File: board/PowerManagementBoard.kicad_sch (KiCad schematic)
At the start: 0 parts

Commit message: Added Hierarchys
Voltage sensing sheet
Reverse Current Protection Sheet
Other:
- added sheet Current Protection (CurrentProtection.kicad_sch)
- added sheet Voltage Sensing (Voltage_Sensing.kicad_sch)
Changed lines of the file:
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@@
 	(generator_version "9.0")
 	(paper "A4")
+	(sheet
+		(at 22.86 72.39)
+		(size 44.45 33.02)
+		(exclude_from_sim no)
+		(in_bom yes)
+		(on_board yes)
+		(dnp no)
+		(fields_autoplaced yes)
+		(stroke
+			(width 0.1524)
+			(type solid)
+		)
+		(fill
+			(color 0 0 0 0.0000)
+		)
+		(property "Sheetname" "Voltage Sensing"
+			(at 22.86 71.6784 0)
+			(effects
+				(font
+					(size 1.27 1.27)
+				)
+				(justify left bottom)
+			)
+		)
+		(property "Sheetfile" "Voltage_Sensing.kicad_sch"
+			(at 22.86 105.9946 0)
+			(effects
+				(font
+					(size 1.27 1.27)
+				)
+				(justify left top)
+			)
+		)
+		(instances
+			(project "PowerManagementBoard"
+				(path "/7eaa639d-7062-45e7-be05-1c2855431307"
+					(page "3")
+				)
+			)
+		)
+	)
+	(sheet
+		(at 21.59 25.4)
+		(size 45.72 33.02)
+		(exclude_from_sim no)
+		(in_bom yes)
+		(on_board yes)
+		(dnp no)
+		(fields_autoplaced yes)
+		(stroke
+			(width 0.1524)
+			(type solid)
+		)
+		(fill
+			(color 0 0 0 0.0000)
+		)
+		(property "Sheetname" "Current Protection"
+			(at 21.59 24.6884 0)
+			(effects
+				(font
+					(size 1.27 1.27)
+				)
+				(justify left bottom)
+			)
+		)
+		(property "Sheetfile" "CurrentProtection.kicad_sch"
+			(at 21.59 59.0046 0)
+			(effects
+				(font
+					(size 1.27 1.27)
+				)
+				(justify left top)
+			)
+		)
+		(instances
+			(project "PowerManagementBoard"
+				(path "/7eaa639d-7062-45e7-be05-1c2855431307"
+					(page "2")
+				)
+			)
+		)
+	)
 	(sheet_instances
 		(path "/"

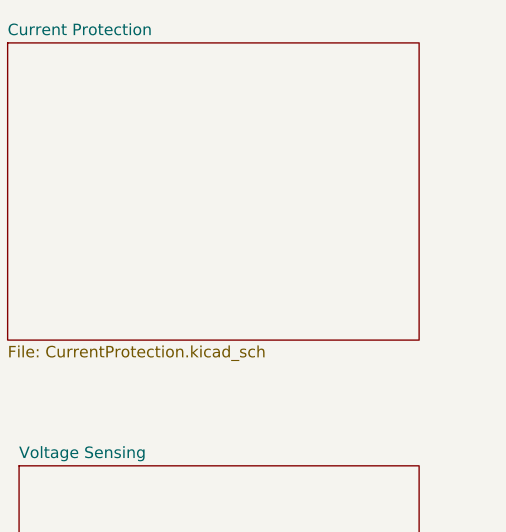
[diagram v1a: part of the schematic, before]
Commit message: Resistor Values
Added resistor values for everything on voltage sensing circuit
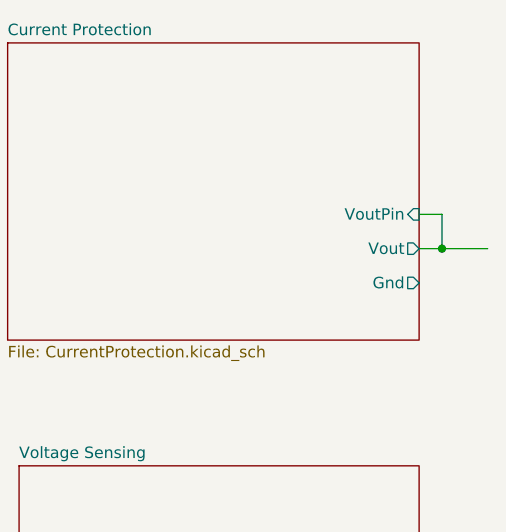
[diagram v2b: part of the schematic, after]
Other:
- sheet Current Protection ports: added Gnd, Vout, VoutPin; removed none
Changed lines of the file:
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@@
 	(generator_version "9.0")
 	(paper "A4")
+	(junction
+		(at 69.85 48.26)
+		(diameter 0)
+		(color 0 0 0 0)
+	)
+	(wire
+		(pts
+			(xy 69.85 48.26) (xy 69.85 44.45)
+		)
+		(stroke
+			(width 0)
+			(type default)
+		)
+	)
+	(wire
+		(pts
+			(xy 67.31 48.26) (xy 69.85 48.26)
+		)
+		(stroke
+			(width 0)
+			(type default)
+		)
+	)
+	(wire
+		(pts
+			(xy 69.85 48.26) (xy 74.93 48.26)
+		)
+		(stroke
+			(width 0)
+			(type default)
+		)
+	)
+	(wire
+		(pts
+			(xy 69.85 44.45) (xy 67.31 44.45)
+		)
+		(stroke
+			(width 0)
+			(type default)
+		)
+	)
 	(sheet
 		(at 22.86 72.39)
@@
 			)
 		)
+		(pin "Gnd" output
+			(at 67.31 52.07 0)
+			(effects
+				(font
+					(size 1.27 1.27)
+				)
+				(justify right)
+			)
+		)
+		(pin "Vout" output
+			(at 67.31 48.26 0)
+			(effects
+				(font
+					(size 1.27 1.27)
+				)
+				(justify right)
+			)
+		)
+		(pin "VoutPin" input
+			(at 67.31 44.45 0)
+			(effects
+				(font
+					(size 1.27 1.27)
+				)
+				(justify right)
+			)
+		)

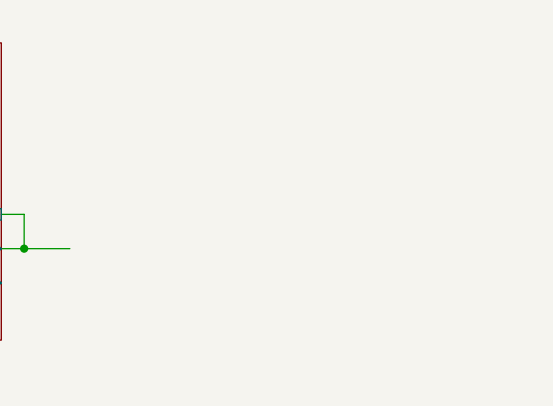
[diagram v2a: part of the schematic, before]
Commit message: fix switch page not showing up
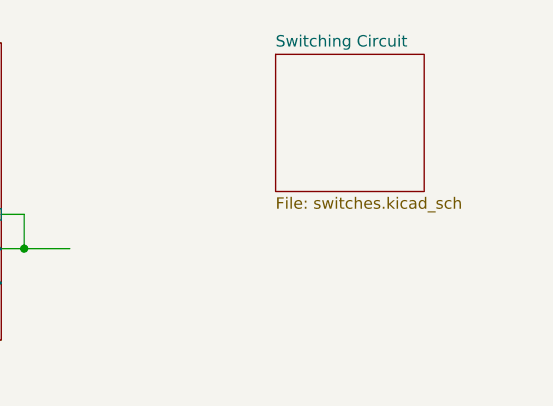
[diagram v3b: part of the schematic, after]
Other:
- added sheet Switching Circuit (switches.kicad_sch)
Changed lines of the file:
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@@
+	)
+	(sheet
+		(at 97.79 26.67)
+		(size 16.51 15.24)
+		(exclude_from_sim no)
+		(in_bom yes)
+		(on_board yes)
+		(dnp no)
+		(fields_autoplaced yes)
+		(stroke
+			(width 0.1524)
+			(type solid)
+		)
+		(fill
+			(color 0 0 0 0.0000)
+		)
+		(property "Sheetname" "Switching Circuit"
+			(at 97.79 25.9584 0)
+			(effects
+				(font
+					(size 1.27 1.27)
+				)
+				(justify left bottom)
+			)
+		)
+		(property "Sheetfile" "switches.kicad_sch"
+			(at 97.79 42.4946 0)
+			(effects
+				(font
+					(size 1.27 1.27)
+				)
+				(justify left top)
+			)
+		)
+		(instances
+			(project "PowerManagementBoard"
+				(path "/7eaa639d-7062-45e7-be05-1c2855431307"
+					(page "4")
+				)
+			)
+		)
 	)
 	(sheet

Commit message: Changed Flags
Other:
- sheet Current Protection ports: added none; removed Gnd, VoutPin
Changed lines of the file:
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@@
 	(generator_version "9.0")
 	(paper "A4")
-	(junction
-		(at 69.85 48.26)
-		(diameter 0)
-		(color 0 0 0 0)
-	)
-	(wire
-		(pts
-			(xy 69.85 48.26) (xy 69.85 44.45)
-		)
-		(stroke
-			(width 0)
-			(type default)
-		)
-	)
-	(wire
-		(pts
-			(xy 67.31 48.26) (xy 69.85 48.26)
-		)
-		(stroke
-			(width 0)
-			(type default)
-		)
-	)
-	(wire
-		(pts
-			(xy 69.85 48.26) (xy 74.93 48.26)
-		)
-		(stroke
-			(width 0)
-			(type default)
-		)
-	)
-	(wire
-		(pts
-			(xy 69.85 44.45) (xy 67.31 44.45)
-		)
-		(stroke
-			(width 0)
-			(type default)
-		)
-	)
 	(sheet
 		(at 22.86 72.39)
@@
 			)
 		)
-		(pin "Gnd" output
-			(at 67.31 52.07 0)
-			(effects
-				(font
-					(size 1.27 1.27)
-				)
-				(justify right)
-			)
-		)
 		(pin "Vout" output
 			(at 67.31 48.26 0)
 			(effects
 				(font
-					(size 1.27 1.27)
-				)
-				(justify right)
-			)
-		)
-		(pin "VoutPin" input
-			(at 67.31 44.45 0)
-			(effects
-				(font

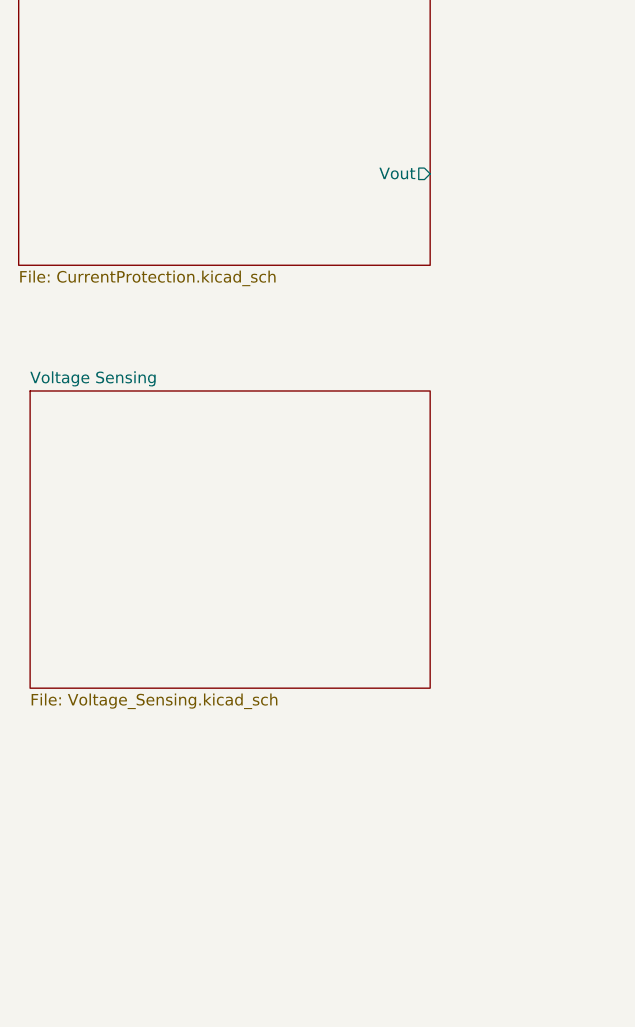
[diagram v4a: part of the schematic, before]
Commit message: Current Sensor in Current Protection
amogus
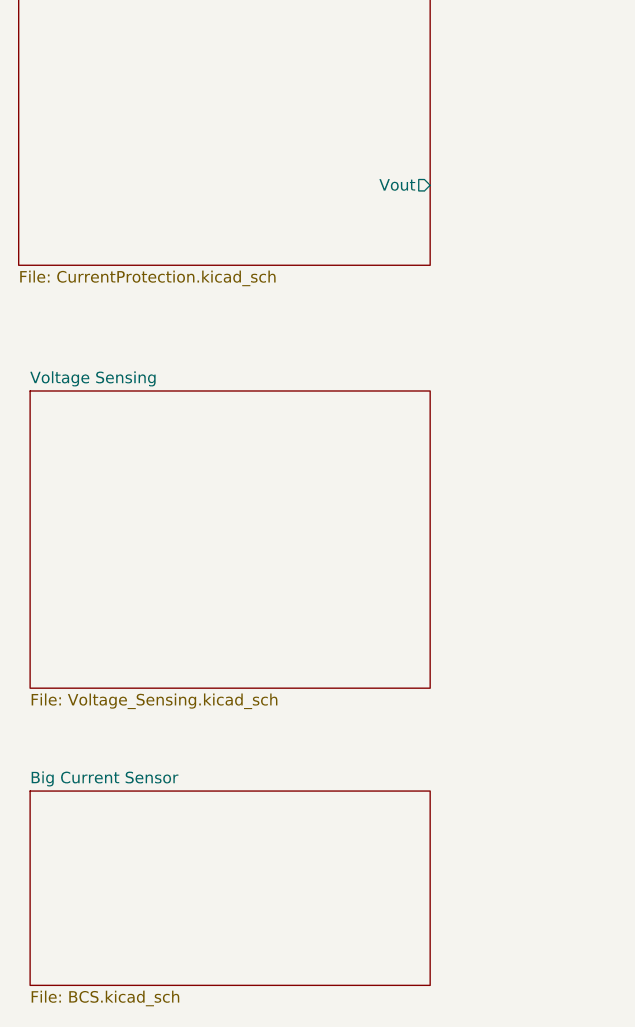
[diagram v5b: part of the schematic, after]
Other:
- added sheet Big Current Sensor (BCS.kicad_sch)
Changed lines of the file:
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@@
+	)
+	(sheet
+		(at 22.86 116.84)
+		(size 44.45 21.59)
+		(exclude_from_sim no)
+		(in_bom yes)
+		(on_board yes)
+		(dnp no)
+		(fields_autoplaced yes)
+		(stroke
+			(width 0.1524)
+			(type solid)
+		)
+		(fill
+			(color 0 0 0 0.0000)
+		)
+		(property "Sheetname" "Big Current Sensor"
+			(at 22.86 116.1284 0)
+			(effects
+				(font
+					(size 1.27 1.27)
+				)
+				(justify left bottom)
+			)
+		)
+		(property "Sheetfile" "BCS.kicad_sch"
+			(at 22.86 139.0146 0)
+			(effects
+				(font
+					(size 1.27 1.27)
+				)
+				(justify left top)
+			)
+		)
+		(instances
+			(project "PowerManagementBoard"
+				(path "/7eaa639d-7062-45e7-be05-1c2855431307"
+					(page "5")
+				)
+			)
+		)
 	)
 	(sheet
@@
 		)
 		(pin "Vout" output
-			(at 67.31 48.26 0)
+			(at 67.31 49.53 0)
 			(effects
 				(font

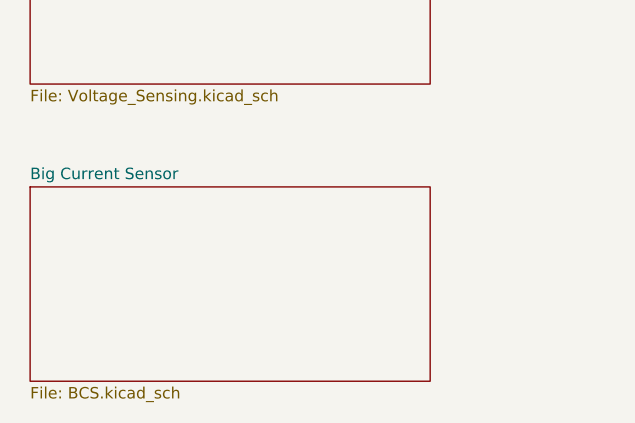
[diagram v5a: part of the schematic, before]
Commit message: make big current sensor go bye bye
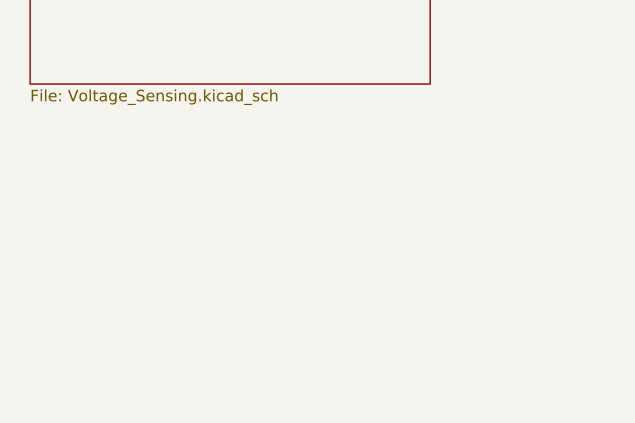
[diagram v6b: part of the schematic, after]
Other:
- removed sheet Big Current Sensor
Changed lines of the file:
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@@
-	)
-	(sheet
-		(at 22.86 116.84)
-		(size 44.45 21.59)
-		(exclude_from_sim no)
-		(in_bom yes)
-		(on_board yes)
-		(dnp no)
-		(fields_autoplaced yes)
-		(stroke
-			(width 0.1524)
-			(type solid)
-		)
-		(fill
-			(color 0 0 0 0.0000)
-		)
-		(property "Sheetname" "Big Current Sensor"
-			(at 22.86 116.1284 0)
-			(effects
-				(font
-					(size 1.27 1.27)
-				)
-				(justify left bottom)
-			)
-		)
-		(property "Sheetfile" "BCS.kicad_sch"
-			(at 22.86 139.0146 0)
-			(effects
-				(font
-					(size 1.27 1.27)
-				)
-				(justify left top)
-			)
-		)
-		(instances
-			(project "PowerManagementBoard"
-				(path "/7eaa639d-7062-45e7-be05-1c2855431307"
-					(page "5")
-				)
-			)
-		)
 	)
 	(sheet

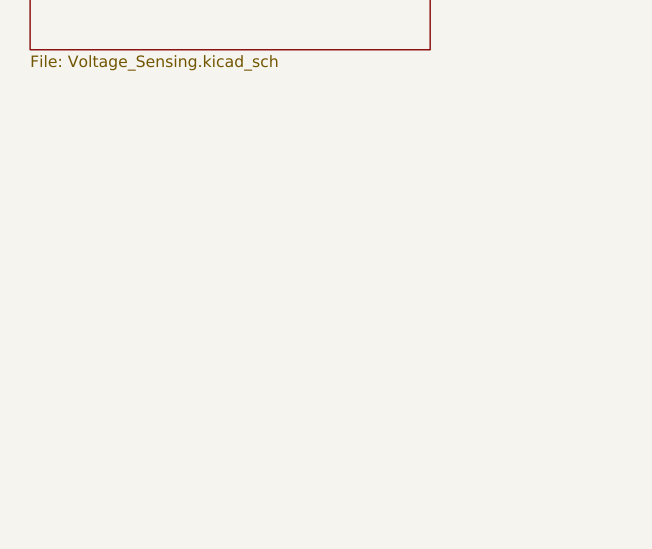
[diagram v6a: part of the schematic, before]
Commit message: added buzzer circuit
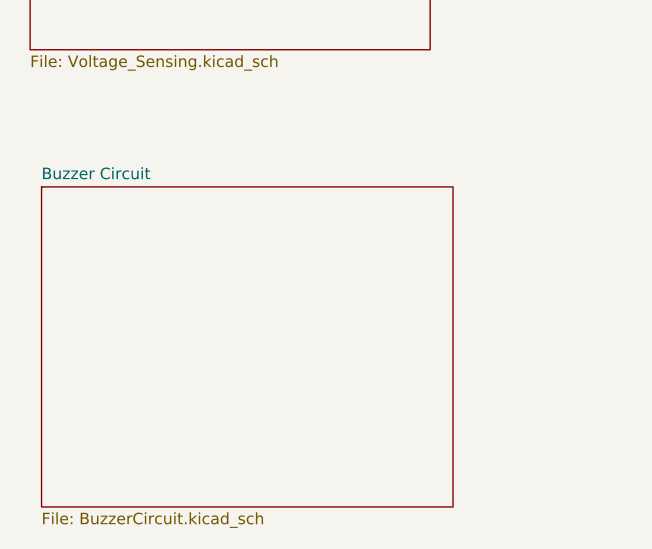
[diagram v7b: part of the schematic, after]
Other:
- added sheet Buzzer Circuit (BuzzerCircuit.kicad_sch)
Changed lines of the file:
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@@
+	)
+	(sheet
+		(at 24.13 120.65)
+		(size 45.72 35.56)
+		(exclude_from_sim no)
+		(in_bom yes)
+		(on_board yes)
+		(dnp no)
+		(fields_autoplaced yes)
+		(stroke
+			(width 0.1524)
+			(type solid)
+		)
+		(fill
+			(color 0 0 0 0.0000)
+		)
+		(property "Sheetname" "Buzzer Circuit"
+			(at 24.13 119.9384 0)
+			(effects
+				(font
+					(size 1.27 1.27)
+				)
+				(justify left bottom)
+			)
+		)
+		(property "Sheetfile" "BuzzerCircuit.kicad_sch"
+			(at 24.13 156.7946 0)
+			(effects
+				(font
+					(size 1.27 1.27)
+				)
+				(justify left top)
+			)
+		)
+		(instances
+			(project "PowerManagementBoard"
+				(path "/7eaa639d-7062-45e7-be05-1c2855431307"
+					(page "5")
+				)
+			)
+		)
 	)
 	(sheet

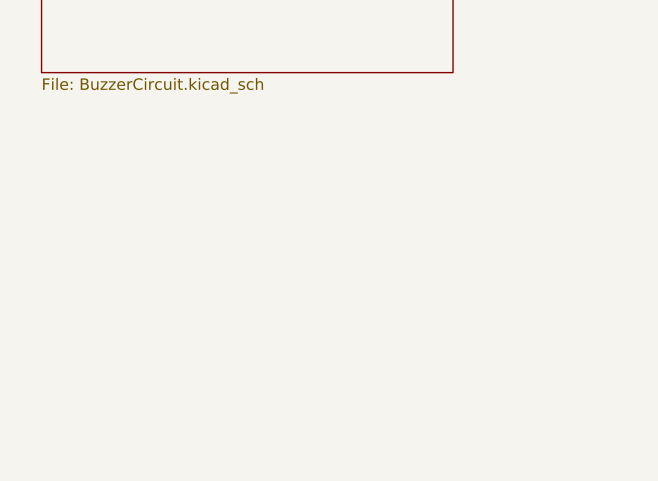
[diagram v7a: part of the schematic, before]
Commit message: Add MCU[WIP] and Ethernet
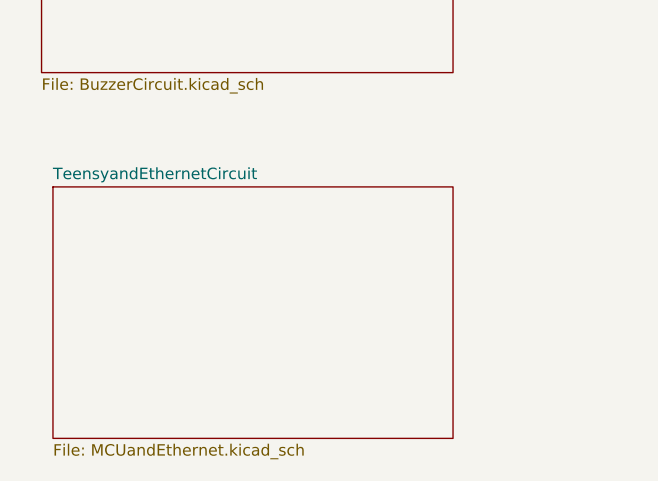
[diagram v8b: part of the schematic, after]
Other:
- added sheet TeensyandEthernetCircuit (MCUandEthernet.kicad_sch)
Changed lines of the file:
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@@
 	(paper "A4")
+	(sheet
+		(at 25.4 168.91)
+		(size 44.45 27.94)
+		(exclude_from_sim no)
+		(in_bom yes)
+		(on_board yes)
+		(dnp no)
+		(fields_autoplaced yes)
+		(stroke
+			(width 0.1524)
+			(type solid)
+		)
+		(fill
+			(color 0 0 0 0.0000)
+		)
+		(property "Sheetname" "TeensyandEthernetCircuit"
+			(at 25.4 168.1984 0)
+			(effects
+				(font
+					(size 1.27 1.27)
+				)
+				(justify left bottom)
+			)
+		)
+		(property "Sheetfile" "MCUandEthernet.kicad_sch"
+			(at 25.4 197.4346 0)
+			(effects
+				(font
+					(size 1.27 1.27)
+				)
+				(justify left top)
+			)
+		)
+		(instances
+			(project "PowerManagementBoard"
+				(path "/7eaa639d-7062-45e7-be05-1c2855431307"
+					(page "6")
+				)
+			)
+		)
+	)
 	(sheet
 		(at 22.86 72.39)
